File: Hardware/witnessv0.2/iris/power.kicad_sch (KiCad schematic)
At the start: 46 parts, among them Q1 SQA403EJ, Q2 SQA403EJ, U2 TPS63070, U3 INA2180A3IDSG, U6 TPS63070

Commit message: iris rework
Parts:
- removed C12, C13, C14, C23, C24, C25: 22u, Capacitor_SMD:C_0805_2012Metric, symbol Device:C_Small
- removed C15, C16, C21, C34, C7: 100n, Capacitor_SMD:C_0402_1005Metric, symbol Device:C_Small
- removed C17: 470n, Capacitor_SMD:C_0603_1608Metric, symbol Device:C_Small
- removed C18, C19: 10u, Capacitor_SMD:C_0805_2012Metric, symbol Device:C_Small
- removed C20, C22, C8, C9: 10u, Capacitor_SMD:C_0603_1608Metric, symbol Device:C_Small
- removed D3: LED, LED_SMD:LED_0603_1608Metric, symbol Device:LED
- removed L1, L3: 1u, Inductor_SMD:L_1210_3225Metric, symbol Device:L
- removed L2: 2.2u, Inductor_SMD:L_Coilcraft_LPS3010, symbol Device:L_Small
- removed R1, R9: 100k, Resistor_SMD:R_0402_1005Metric, symbol Device:R_Small
- removed R10, R12, R6: 10k, Resistor_SMD:R_0402_1005Metric, symbol Device:R_Small
- removed R11: 35k, Resistor_SMD:R_0402_1005Metric, symbol Device:R_Small
- removed R2: 470k, Resistor_SMD:R_0402_1005Metric, symbol Device:R_Small
- removed R3: 150k, Resistor_SMD:R_0402_1005Metric, symbol Device:R_Small
- removed R33, R34: 2.5m, Resistor_SMD:R_0603_1608Metric, symbol Device:R_Small
- removed R5: 4.7, Resistor_SMD:R_0402_1005Metric, symbol Device:R_Small
- removed R7: 680k, Resistor_SMD:R_0402_1005Metric, symbol Device:R_Small
- removed R8: 130k, Resistor_SMD:R_0402_1005Metric, symbol Device:R_Small
- removed U2, U6: TPS63070, Witness:RNM0015A, symbol Witness:TPS63070
- removed U3: INA2180A3IDSG, Package_SON:Texas_DSG0008A_WSON-8-1EP_2x2mm_P0.5mm_EP0.9x1.6mm_ThermalVias, symbol Amplifier_Current:INA2180AxxDSG
- added R32: 1k, Resistor_SMD:R_0402_1005Metric, symbol Device:R_Small
- added U2: ME6118A33PG, Package_TO_SOT_SMD:SOT-89-3, symbol Witness:ME6118A33B3G
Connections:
- net +3V3: now also C11.1, U2.2 (VOUT)
- net +BATT: now also C10.1, D4.1 (K), Q2.4 (S), R21.2, U2.3 (VIN); no longer Q2.1 (D)
- net GND: now also R32.1, U2.1 (GND); no longer R21.1
- removed net BATT_POSTSW: C10.1, C11.1
- net ISENSE+: no longer names the net of Q1.4 (S)
- net ISENSE+: now also Q2.1 (D)
- new net BATT_RAW: Q1.1 (D)
- new net VSENSE: R21.1, R32.2
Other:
- note added: "3v3 Rail - 500mA continuous, 1A peak"
- note removed: "3v3 Rail - 500mA continuous, 1.3A peak"
- note removed: "5v Rail - 1.25A continuous"
- note removed: "Current Sense"
- note removed: "Output Filter"
- moved on the sheet: C10, D2, D4, Q2, R20

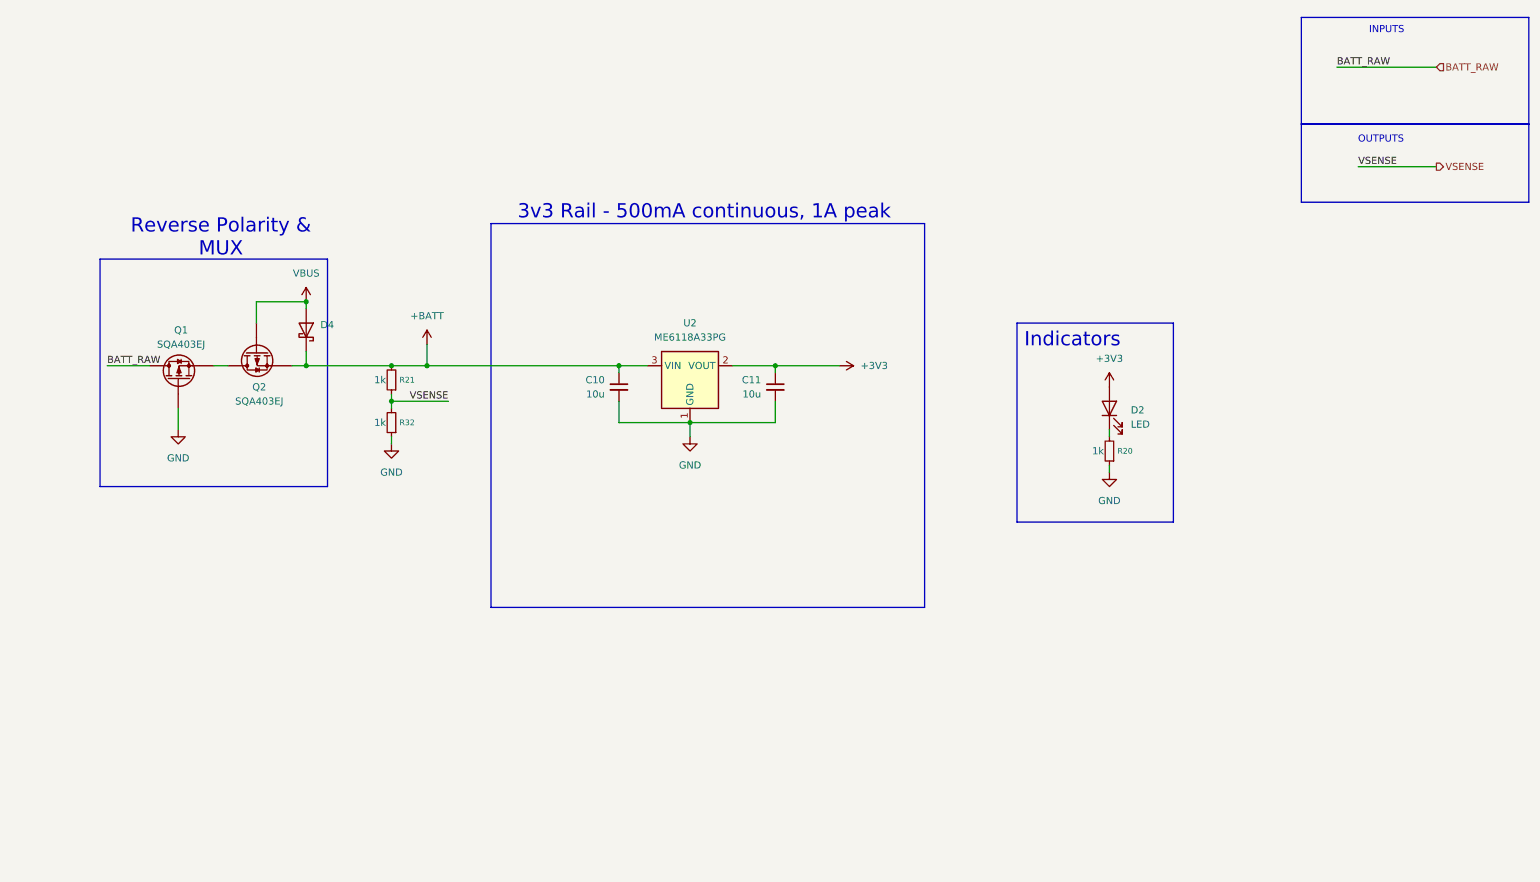
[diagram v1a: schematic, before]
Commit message: trying to make cam board
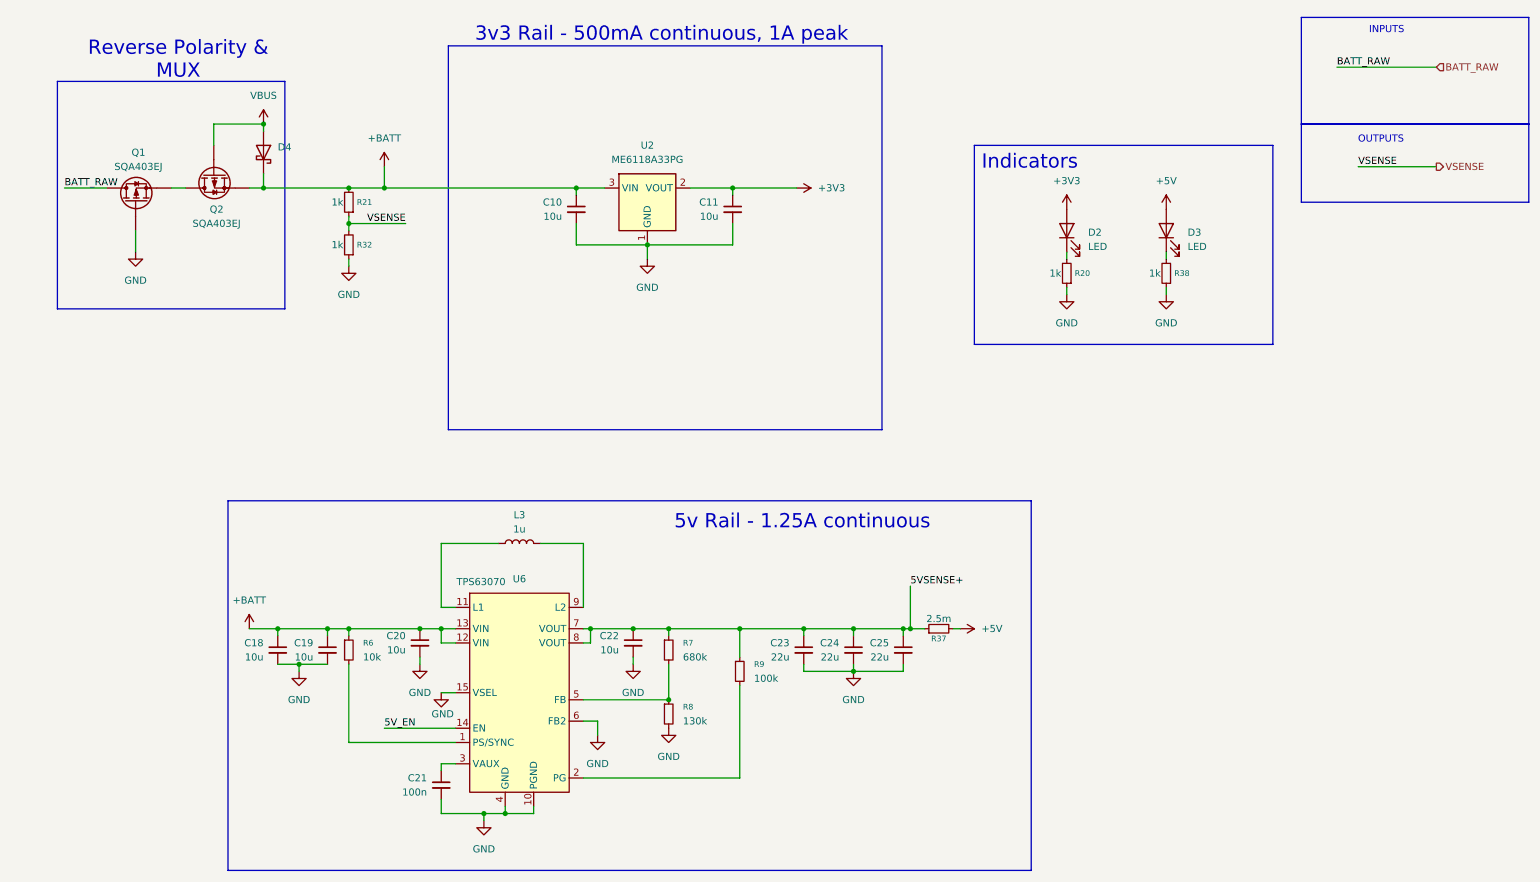
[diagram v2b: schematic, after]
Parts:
- added C18, C19: 10u, Capacitor_SMD:C_0805_2012Metric, symbol Device:C_Small
- added C20, C22: 10u, Capacitor_SMD:C_0603_1608Metric, symbol Device:C_Small
- added C21: 100n, Capacitor_SMD:C_0402_1005Metric, symbol Device:C_Small
- added C23, C24, C25: 22u, Capacitor_SMD:C_0805_2012Metric, symbol Device:C_Small
- added D3: LED, LED_SMD:LED_0603_1608Metric, symbol Device:LED
- added L3: 1u, Inductor_SMD:L_1210_3225Metric, symbol Device:L
- added R37: 2.5m, Resistor_SMD:R_0603_1608Metric, symbol Device:R_Small
- added R38: 1k, Resistor_SMD:R_0402_1005Metric, symbol Device:R_Small
- added R6: 10k, Resistor_SMD:R_0402_1005Metric, symbol Device:R_Small
- added R7: 680k, Resistor_SMD:R_0402_1005Metric, symbol Device:R_Small
- added R8: 130k, Resistor_SMD:R_0402_1005Metric, symbol Device:R_Small
- added R9: 100k, Resistor_SMD:R_0402_1005Metric, symbol Device:R_Small
- added U6: TPS63070, Witness:RNM0015A, symbol Witness:TPS63070
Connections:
- net +BATT: now also C18.1, C19.1, C20.1, R6.1, U6.12 (VIN), U6.13 (VIN)
- net GND: now also C18.2, C19.2, C20.2, C21.2, C22.2, C23.2, C24.2, C25.2, R38.1, R8.2, U6.10 (PGND), U6.15 (VSEL), U6.4 (GND), U6.6 (FB2)
- new net: D3.1 (K), R38.2
- new net: R9.2, U6.2 (PG)
- new net: R7.2, R8.1, U6.5 (FB)
- new net: R6.2, U6.1 (PS/SYNC)
- new net: C21.1, U6.3 (VAUX)
- new net: L3.1, U6.11 (L1)
- new net: L3.2, U6.9 (L2)
- new net +5V: D3.2 (A), R37.2
- new net 5VSENSE+: C22.1, C23.1, C24.1, C25.1, R37.1, R7.1, R9.1, U6.7 (VOUT), U6.8 (VOUT)
- new net 5V_EN: U6.14 (EN)
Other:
- note added: "5v Rail - 1.25A continuous"
- moved on the sheet: C10, C11, D2, D4, Q1, Q2, R20, R21, R32, U2

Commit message: iris inital layout
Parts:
- removed R37: 2.5m, Resistor_SMD:R_0603_1608Metric, symbol Device:R_Small
- added D5: BZX584C10, Diode_SMD:D_SOD-523, symbol Device:D_Zener_Small
- added R10: 10k, Resistor_SMD:R_0402_1005Metric, symbol Device:R_Small
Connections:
- net 5VSENSE+ is gone; now on net +5V: C22.1, C23.1, C24.1, C25.1, R7.1, R9.1, U6.7 (VOUT), U6.8 (VOUT)
- net GND: now also R10.2; no longer Q1.3 (G)
- net at Q1.4 (S), Q2.1 (D): now also D5.1 (K)
- new net: D5.2 (A), Q1.3 (G), R10.1
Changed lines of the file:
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@@
 	)
 	(junction
-		(at 172.72 121.92)
-		(diameter 0)
-		(color 0 0 0 0)
-	)
-	(junction
 		(at 142.24 121.92)
 		(diameter 0)
@@
 	)
 	(junction
+		(at 41.91 43.18)
+		(diameter 0)
+		(color 0 0 0 0)
+	)
+	(junction
+		(at 34.29 50.8)
+		(diameter 0)
+		(color 0 0 0 0)
+	)
+	(junction
 		(at 100.33 154.94)
 		(diameter 0)
@@
 	(wire
 		(pts
+			(xy 34.29 50.8) (xy 41.91 50.8)
+		)
+		(stroke
+			(width 0)
+			(type default)
+		)
+	)
+	(wire
+		(pts
 			(xy 162.56 129.54) (xy 171.45 129.54)
 		)
@@
 	(wire
 		(pts
-			(xy 172.72 121.92) (xy 175.26 121.92)
+			(xy 171.45 121.92) (xy 181.61 121.92)
 		)
 		(stroke
@@
 	(wire
 		(pts
-			(xy 40.64 43.18) (xy 43.18 43.18)
+			(xy 40.64 43.18) (xy 41.91 43.18)
 		)
 		(stroke
@@
 	(wire
 		(pts
-			(xy 34.29 50.8) (xy 34.29 54.61)
+			(xy 34.29 50.8) (xy 34.29 53.34)
 		)
 		(stroke
@@
 	(wire
 		(pts
+			(xy 248.92 25.4) (xy 266.7 25.4)
+		)
+		(stroke
+			(width 0)
+			(type default)
+		)
+	)
+	(wire
+		(pts
 			(xy 115.57 121.92) (xy 114.3 121.92)
 		)
@@
 	(wire
 		(pts
+			(xy 41.91 43.18) (xy 41.91 45.72)
+		)
+		(stroke
+			(width 0)
+			(type default)
+		)
+	)
+	(wire
+		(pts
 			(xy 63.5 128.27) (xy 59.69 128.27)
 		)
@@
 	(wire
 		(pts
-			(xy 172.72 114.3) (xy 172.72 121.92)
-		)
-		(stroke
-			(width 0)
-			(type default)
-		)
-	)
-	(wire
-		(pts
 			(xy 54.61 43.18) (xy 57.15 43.18)
 		)
@@
 	(wire
 		(pts
-			(xy 171.45 121.92) (xy 172.72 121.92)
+			(xy 41.91 43.18) (xy 43.18 43.18)
 		)
 		(stroke
@@
 	(wire
 		(pts
-			(xy 180.34 121.92) (xy 181.61 121.92)
-		)
-		(stroke
-			(width 0)
-			(type default)
-		)
-	)
-	(wire
-		(pts
 			(xy 200.66 54.61) (xy 200.66 55.88)
 		)
@@
 		)
 	)
-	(label "VSENSE"
-		(at 252.73 39.37 0)
+	(label "5V_EN"
+		(at 248.92 25.4 0)
 		(effects
 			(font
@@
 		)
 	)
-	(label "5VSENSE+"
-		(at 172.72 114.3 0)
+	(label "VSENSE"
+		(at 252.73 39.37 0)
 		(effects
 			(font
@@
 		)
 	)
+	(hierarchical_label "5V_EN"
+		(shape input)
+		(at 266.7 25.4 0)
+		(effects
+			(font
+				(size 1.27 1.27)
+			)
+			(justify left)
+		)
+	)
 	(hierarchical_label "VSENSE"
 		(shape output)
@@
 	)
 	(symbol
+		(lib_id "Device:D_Zener_Small")
+		(at 41.91 48.26 90)
+		(mirror x)
+		(unit 1)
+		(body_style 1)
+		(exclude_from_sim no)
+		(in_bom yes)
+		(on_board yes)
+		(in_pos_files yes)
+		(dnp no)
+		(property "Reference" "D5"
+			(at 39.37 46.9899 90)
+			(show_name no)
+			(do_not_autoplace no)
+			(effects
+				(font
+					(size 1.27 1.27)
+				)
+				(justify left)
+			)
+		)
+		(property "Value" "BZX584C10"
+			(at 39.37 49.5299 90)
+			(hide yes)
+			(show_name no)
+			(do_not_autoplace no)
+			(effects
+				(font
+					(size 1.27 1.27)
+				)
+				(justify left)
+			)
+		)
+		(property "Footprint" "Diode_SMD:D_SOD-523"
+			(at 41.91 48.26 90)
+			(hide yes)
+			(show_name no)
+			(do_not_autoplace no)
+			(effects
+				(font
+					(size 1.27 1.27)
+				)
+			)
+		)
+		(property "Datasheet" ""
+			(at 41.91 48.26 90)
+			(hide yes)
+			(show_name no)
+			(do_not_autoplace no)
+			(effects
+				(font
+					(size 1.27 1.27)
+				)
+			)
+		)
+		(property "Description" "Zener diode, small symbol"
+			(at 41.91 48.26 0)
+			(hide yes)
+			(show_name no)
+			(do_not_autoplace no)
+			(effects
+				(font
+					(size 1.27 1.27)
+				)
+			)
+		)
+		(property "LCSC_Part" "C22395577"
+			(at 41.91 48.26 90)
+			(hide yes)
+			(show_name no)
+			(do_not_autoplace no)
+			(effects
+				(font
+					(size 1.27 1.27)
+				)
+			)
+		)
+		(pin "2"
+		)
+		(pin "1"
+		)
+		(instances
+			(project "iris"
+				(path "/c7e4a338-55e7-4896-822a-22161197db9b/e1fc9771-294d-4cbf-8437-96abea4a6606"
+					(reference "D5")
+					(unit 1)
+				)
+			)
+		)
+	)
+	(symbol
 		(lib_id "power:+BATT")
 		(at 78.74 39.37 0)
@@
 	)
 	(symbol
-		(lib_id "Device:R_Small")
-		(at 177.8 121.92 90)
-		(unit 1)
-		(body_style 1)
-		(exclude_from_sim no)
-		(in_bom yes)
-		(on_board yes)
-		(in_pos_files yes)
-		(dnp no)
-		(property "Reference" "R37"
-			(at 177.8 123.698 90)
-			(show_name no)
-			(do_not_autoplace no)
-			(effects
-				(font
-					(size 1.016 1.016)
-				)
-			)
-		)
-		(property "Value" "2.5m"
-			(at 177.8 120.142 90)
-			(show_name no)
-			(do_not_autoplace no)
-			(effects
-				(font
-					(size 1.27 1.27)
-				)
-			)
-		)
-		(property "Footprint" "Resistor_SMD:R_0603_1608Metric"
-			(at 177.8 121.92 0)
-			(hide yes)
-			(show_name no)
-			(do_not_autoplace no)
-			(effects
-				(font
-					(size 1.27 1.27)
-				)
-			)
-		)
-		(property "Datasheet" ""
-			(at 177.8 121.92 0)
-			(hide yes)
-			(show_name no)
-			(do_not_autoplace no)
-			(effects
-				(font
-					(size 1.27 1.27)
-				)
-			)
-		)
-		(property "Description" "Resistor, small symbol"
-			(at 177.8 121.92 0)
-			(hide yes)
-			(show_name no)
-			(do_not_autoplace no)
-			(effects
-				(font
-					(size 1.27 1.27)
-				)
-			)
-		)
-		(property "LCSC_Part" "C42758536"
-			(at 177.8 121.92 90)
-			(hide yes)
-			(show_name no)
-			(do_not_autoplace no)
-			(effects
-				(font
-					(size 1.27 1.27)
-				)
-			)
-		)
-		(pin "2"
-		)
-		(pin "1"
-		)
-		(instances
-			(project "iris"
-				(path "/c7e4a338-55e7-4896-822a-22161197db9b/e1fc9771-294d-4cbf-8437-96abea4a6606"
-					(reference "R37")
-					(unit 1)
-				)
-			)
-		)
-	)
-	(symbol
 		(lib_id "Device:C_Small")
 		(at 88.9 149.86 0)
@@
 	(symbol
 		(lib_id "power:GND")
-		(at 34.29 54.61 0)
+		(at 34.29 58.42 0)
 		(unit 1)
 		(body_style 1)
@@
 		(fields_autoplaced yes)
 		(property "Reference" "#PWR016"
-			(at 34.29 60.96 0)
+			(at 34.29 64.77 0)
 			(hide yes)
 			(show_name no)
@@
 		)
 		(property "Value" "GND"
-			(at 34.29 59.69 0)
+			(at 34.29 63.5 0)
 			(show_name no)
 			(do_not_autoplace no)
@@
 		)
 		(property "Footprint" ""
-			(at 34.29 54.61 0)
+			(at 34.29 58.42 0)
 			(hide yes)
 			(show_name no)
@@
 		)
 		(property "Datasheet" ""
-			(at 34.29 54.61 0)
+			(at 34.29 58.42 0)
 			(hide yes)
 			(show_name no)
@@
 		)
 		(property "Description" "Power symbol creates a global label with name \"GND\" , ground"
-			(at 34.29 54.61 0)
+			(at 34.29 58.42 0)
 			(hide yes)
 			(show_name no)
@@
 					(unit 1)
 				)
+			)
+		)
+	)
+	(symbol
+		(lib_id "Device:R_Small")
+		(at 34.29 55.88 0)
+		(unit 1)
+		(body_style 1)
+		(exclude_from_sim no)
+		(in_bom yes)
+		(on_board yes)
+		(in_pos_files yes)
+		(dnp no)
+		(fields_autoplaced yes)
+		(property "Reference" "R10"
+			(at 36.83 54.6099 0)
+			(show_name no)
+			(do_not_autoplace no)
+			(effects
+				(font
+					(size 1.016 1.016)
+				)
+				(justify left)
+			)
+		)
+		(property "Value" "10k"
+			(at 36.83 57.1499 0)
+			(show_name no)
+			(do_not_autoplace no)
+			(effects
+				(font
+					(size 1.27 1.27)
+				)
+				(justify left)
+			)
+		)
+		(property "Footprint" "Resistor_SMD:R_0402_1005Metric"
+			(at 34.29 55.88 0)
+			(hide yes)
+			(show_name no)
+			(do_not_autoplace no)
+			(effects
+				(font
+					(size 1.27 1.27)
+				)
+			)
+		)
+		(property "Datasheet" ""
+			(at 34.29 55.88 0)
+			(hide yes)
+			(show_name no)
+			(do_not_autoplace no)
+			(effects
+				(font
+					(size 1.27 1.27)
+				)
+			)
+		)
+		(property "Description" "Resistor, small symbol"
+			(at 34.29 55.88 0)
+			(hide yes)
+			(show_name no)
+			(do_not_autoplace no)
+			(effects
+				(font
+					(size 1.27 1.27)
+				)
+			)
+		)
+		(property "LCSC_Part" "C25744"
+			(at 34.29 55.88 0)
+			(hide yes)
+			(show_name no)
+			(do_not_autoplace no)
+			(effects
+				(font
+					(size 1.27 1.27)
+				)
+			)
+		)
+		(pin "2"
+		)
+		(pin "1"
+		)
+		(instances
+			(project "iris"
+				(path "/c7e4a338-55e7-4896-822a-22161197db9b/e1fc9771-294d-4cbf-8437-96abea4a6606"
+					(reference "R10")
+					(unit 1)
+				)

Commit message: root feedback
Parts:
- added C12: 10u, Capacitor_SMD:C_0805_2012Metric, symbol Device:C_Small
- R21: value 1k -> 15k; LCSC_Part C11702 -> (none)
- R32: value 1k -> 5k; LCSC_Part C11702 -> (none)
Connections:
- net +3V3: now also C12.1
- net GND: now also C12.2
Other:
- moved on the sheet: C18, C19, C20, C21, C22, C23, C24, C25, L3, R6, R7, R8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
